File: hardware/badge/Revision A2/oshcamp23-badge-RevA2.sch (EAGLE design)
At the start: 58 parts, among them CON2 STEMMA_I2C_QT, IC2 LD1117-3.3, IC3 WMCU-ESP8285H16, J1 61030621121, P1 Buzzer, Q1 SS8050, Q2 SS8050, Q3 SS8050

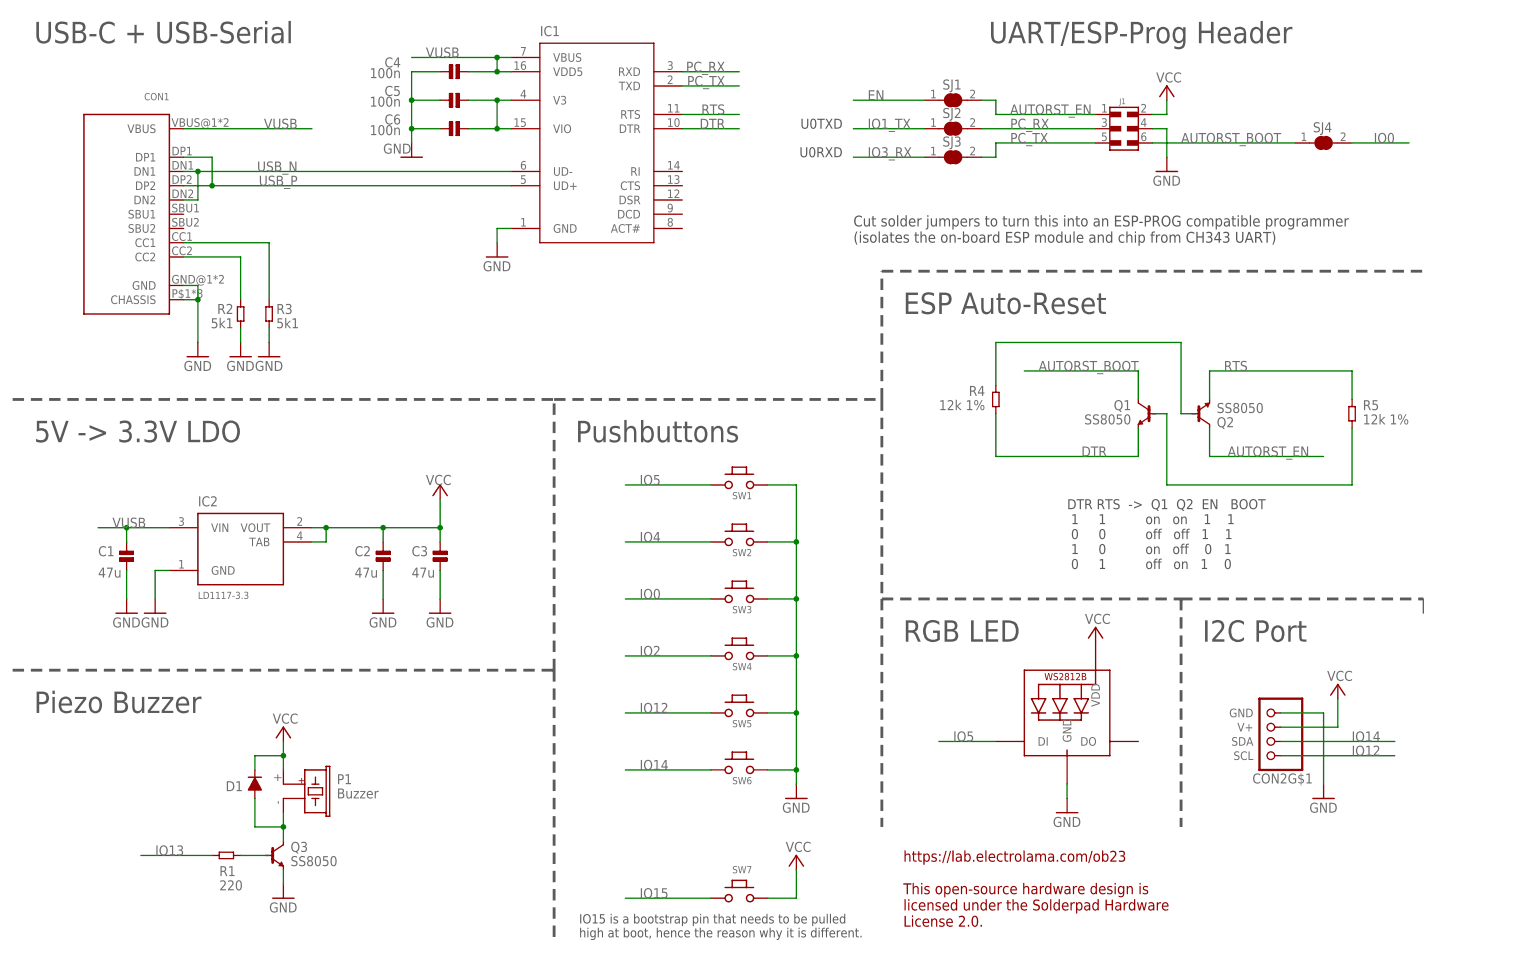
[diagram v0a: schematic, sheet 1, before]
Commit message: add iboms for both kit variants
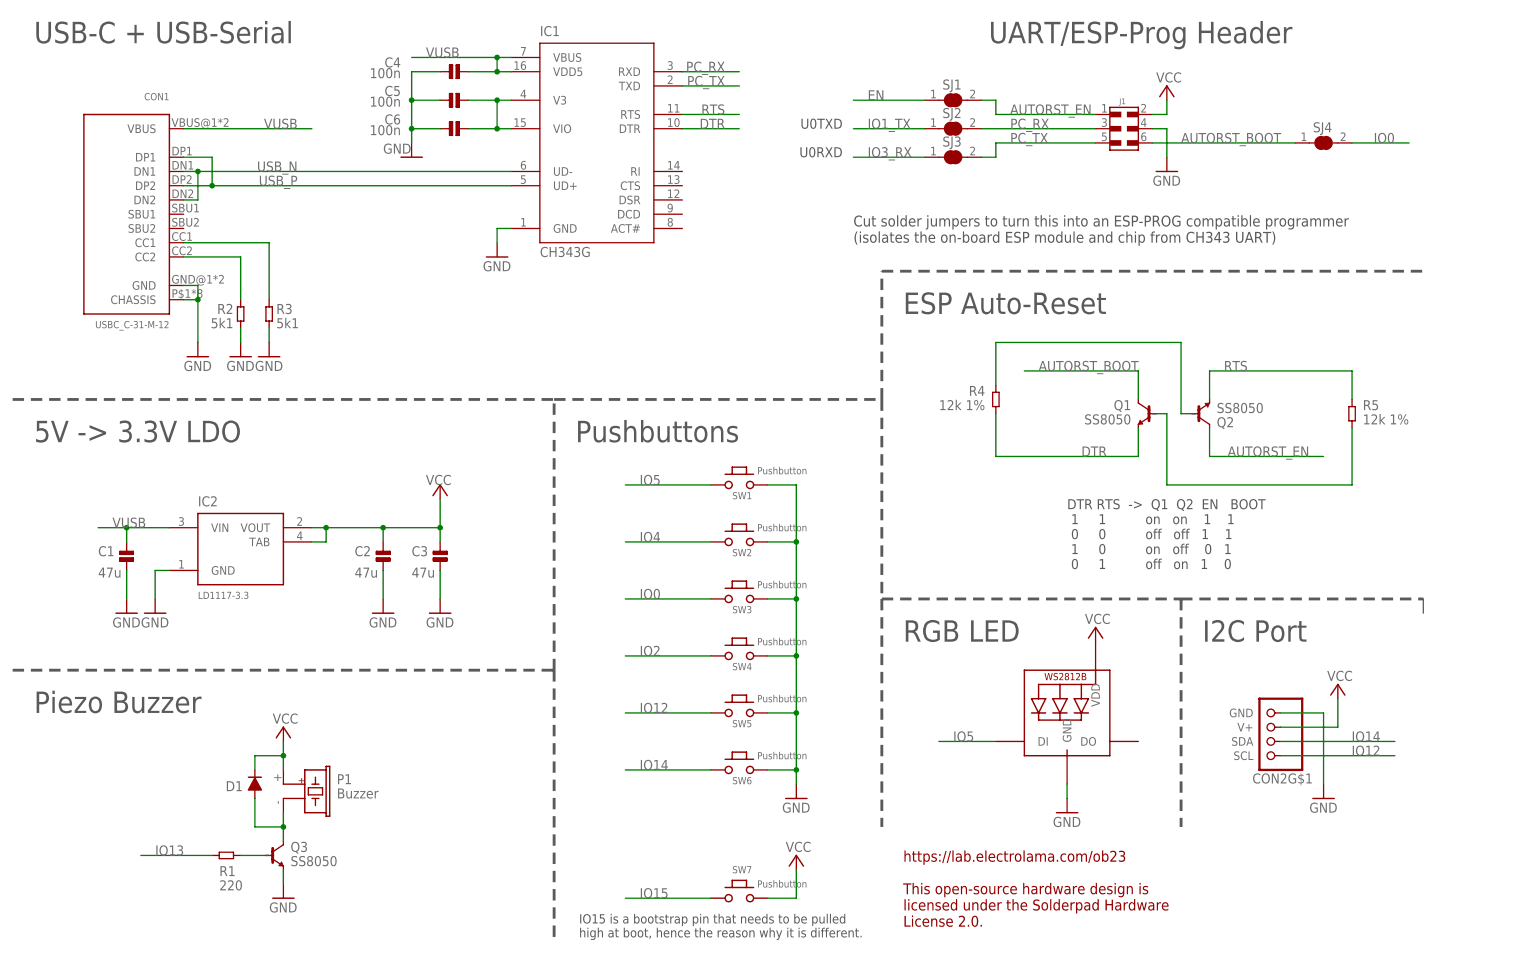
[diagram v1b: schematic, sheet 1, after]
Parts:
- ANT1, C10, C11, C12, C13, C14, C15, C16, C17, C20, C7, IC3, R10, R11, R6, R7, R8, R9, XT1: KIT_EASY (none) -> NO
- C18, C19, MOD1: KIT_HARD (none) -> NO
- C8, C9, D1, SJ1, SJ2, SJ3, SJ4: KIT_EASY (none) -> NO; KIT_HARD (none) -> NO
- CON1: value (none) -> USBC_C-31-M-12
- IC1: value (none) -> CH343G
- L1: value TBD -> 0R LINK (Temp); KIT_EASY (none) -> NO
- SW1, SW2, SW3, SW4, SW5, SW6, SW7: value (none) -> Pushbutton
